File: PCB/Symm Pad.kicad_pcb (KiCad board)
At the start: 2 copper layers, 74 x 64.3 mm, 21 parts, among them J1 0.91"_OLED_Display, SW1 SW_Push, SW2 SW_Push, SW3 SW_Push, SW4 SW_Push, SW5 SW_Push, SW6 SW_Push, SW7 RotaryEncoder_Switch, U1 XIAO-RP2040-DIP

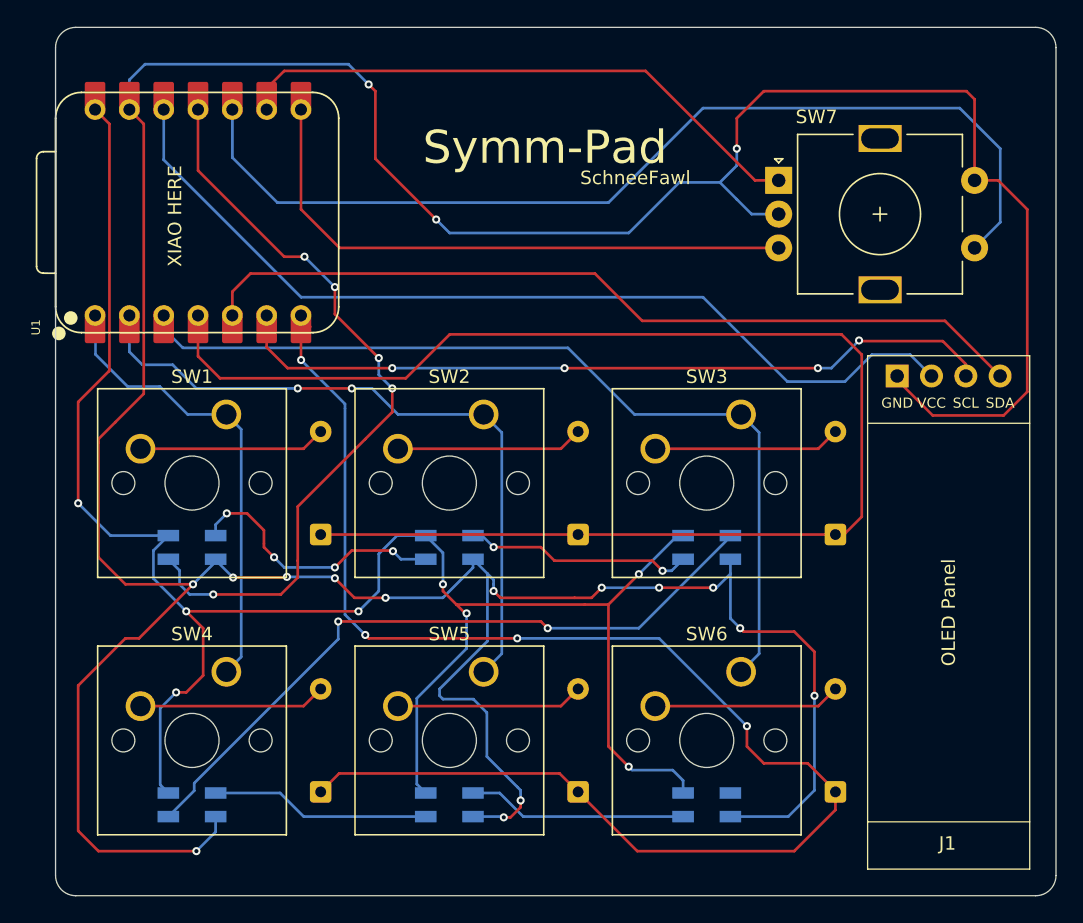
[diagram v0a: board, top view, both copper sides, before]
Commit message: Cleaned up tracks and vias
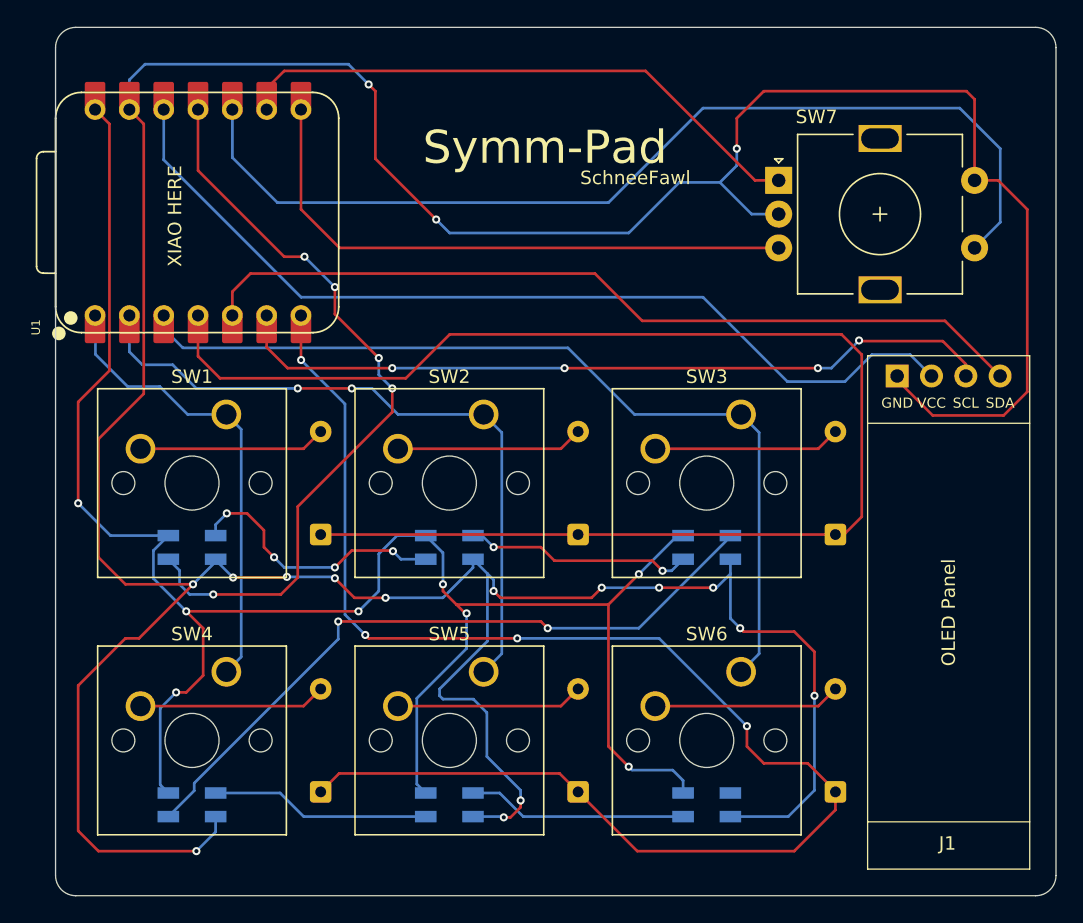
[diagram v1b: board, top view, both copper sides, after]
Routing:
- net Row 1: track 110.5 -> 109.8 mm
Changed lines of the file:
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@@
 	)
 	(segment
-		(start 78.75 55)
+		(start 78.5 55)
 		(end 81.5 55)
 		(width 0.2)
@@
 	)
 	(segment
-		(start 78.5 55)
-		(end 78.75 55)
-		(width 0.2)
-		(layer "F.Cu")
-		(net 1)
-	)
-	(segment
-		(start 72 54.5)
-		(end 72 54.75)
-		(width 0.2)
-		(layer "F.Cu")
-		(net 1)
-	)
-	(segment
 		(start 69.25 52.25)
 		(end 70.75 52.25)
@@
 	(segment
 		(start 72 53.5)
-		(end 72 54.5)
+		(end 72 54.75)
 		(width 0.2)
 		(layer "F.Cu")
@@
 	)
 	(segment
-		(start 59.75 46.75)
-		(end 59.75 47)
-		(width 0.2)
-		(layer "F.Cu")
-		(net 2)
-	)
-	(segment
 		(start 90.25 74.75)
 		(end 89.75 74.75)
@@
 	)
 	(segment
-		(start 61 45.5)
-		(end 59.75 46.75)
-		(width 0.2)
-		(layer "F.Cu")
-		(net 2)
-	)
-	(segment
 		(start 62.04 22.36)
 		(end 63.103 23.423)
@@
 	)
 	(segment
-		(start 63.103 43.397)
-		(end 61 45.5)
+		(start 59.75 46.75)
+		(end 63.103 43.397)
 		(width 0.2)
 		(layer "F.Cu")
@@
 	)
 	(segment
-		(start 95 58.5)
+		(start 89.5 58.5)
 		(end 96.25 58.5)
 		(width 0.2)
@@
 	)
 	(segment
-		(start 59.75 47)
+		(start 59.75 46.75)
 		(end 59.75 55.5)
 		(width 0.2)
@@
 	)
 	(segment
-		(start 89.5 58.5)
-		(end 95 58.5)
-		(width 0.2)
-		(layer "F.Cu")
-		(net 2)
-	)
-	(segment
 		(start 62.75 61.5)
 		(end 61.75 61.5)
@@
 	)
 	(segment
-		(start 90.75 72.5)
+		(start 88.5 70.25)
 		(end 91 72.75)
 		(width 0.2)
@@
 	)
 	(segment
-		(start 107 29)
+		(start 105.75 27.75)
 		(end 108.1 30.1)
 		(width 0.2)
@@
 	)
 	(segment
-		(start 88.5 70.25)
-		(end 90.75 72.5)
-		(width 0.2)
-		(layer "B.Cu")
-		(net 2)
-	)
-	(segment
 		(start 85.25 66)
 		(end 87.5 66)
@@
 	(segment
 		(start 89 57.16875)
-		(end 89 57.5)
-		(width 0.2)
-		(layer "B.Cu")
-		(net 2)
-	)
-	(segment
-		(start 107 29)
-		(end 105.75 27.75)
+		(end 89 58)
 		(width 0.2)
 		(layer "B.Cu")
@@
 	)
 	(segment
-		(start 89 57.5)
-		(end 89 58)
-		(width 0.2)
-		(layer "B.Cu")
-		(net 2)
-	)
-	(segment
 		(start 85 65.75)
 		(end 85.25 66)
@@
 	)
 	(segment
-		(start 86.25 59)
-		(end 95.75 59)
-		(width 0.2)
-		(layer "F.Cu")
-		(net 3)
-	)
-	(segment
-		(start 67.5 61)
+		(start 67.5 60.75)
 		(end 67.5 64.25)
 		(width 0.2)
@@
 	)
 	(segment
-		(start 95.75 59)
+		(start 86.25 59)
 		(end 97.5 59)
 		(width 0.2)
@@
 	)
 	(segment
-		(start 60.563 41.687)
-		(end 60.5 41.75)
+		(start 58.25 44)
+		(end 60.563 41.687)
 		(width 0.2)
 		(layer "F.Cu")
@@
 	)
 	(segment
-		(start 67.5 60.75)
-		(end 67.5 61)
-		(width 0.2)
-		(layer "F.Cu")
-		(net 3)
-	)
-	(segment
 		(start 85.25 58)
 		(end 86.25 59)
@@
 		(net 3)
 	)
-	(segment
-		(start 60.5 41.75)
-		(end 58.25 44)
-		(width 0.2)
-		(layer "F.Cu")
-		(net 3)
-	)
 	(via
 		(at 79 59.5)
@@
 	)
 	(segment
-		(start 74.5 55.75)
+		(start 74.5 51.75)
 		(end 74.5 57)
 		(width 0.2)
@@
 	)
 	(segment
-		(start 81.5 44.75)
-		(end 79.5 46.75)
-		(width 0.2)
-		(layer "F.Cu")
-		(net 4)
-	)
-	(segment
 		(start 67.12 22.36)
 		(end 67.12 26.87)
@@
 	)
 	(segment
-		(start 79.5 46.75)
-		(end 74.5 51.75)
+		(start 74.5 51.75)
+		(end 81.5 44.75)
 		(width 0.2)
 		(layer "F.Cu")
@@
 	)
 	(segment
-		(start 74.5 51.75)
-		(end 74.5 55.75)
-		(width 0.2)
-		(layer "F.Cu")
-		(net 4)
-	)
-	(segment
 		(start 81.5 43)
 		(end 81.5 44.75)
@@
 	)
 	(segment
-		(start 75.435 38.435)
-		(end 74.74 38.435)
-		(width 0.2)
-		(layer "F.Cu")
-		(net 25)
-	)
-	(segment
 		(start 74.75 40.9)
 		(end 74.74 40.89)
@@
 	(segment
 		(start 78 59.75)
-		(end 78 44.5)
+		(end 78 44.15)
 		(width 0.2)
 		(layer "B.Cu")
@@
 		(width 0.2)
 		(layer "B.Cu")
-		(net 25)
-	)
-	(segment
-		(start 78 44.5)
-		(end 78 44.15)
-		(width 0.2)
-		(layer "B.Cu")

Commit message: Correct footprint of neopixels
Earlier the SK6812 MINI footprint was being used which wasn't correct. Now changed to SK6812 MINI-E footprints.
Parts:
- removed D1, D2, D3, D4, D5, D6: SK6812MINI, LED_SMD:LED_SK6812MINI_PLCC4_3.5x3.5mm_P1.75mm
- added D13: SK6812MINI-E, kicad-keyboard-parts:MX_SK6812MINI-E, F.Cu at (66.7, 50.0)
- added D14: SK6812MINI-E, kicad-keyboard-parts:MX_SK6812MINI-E, F.Cu at (85.7, 50.0)
- added D15: SK6812MINI-E, kicad-keyboard-parts:MX_SK6812MINI-E, F.Cu at (104.8, 50.0)
- added D16: SK6812MINI-E, kicad-keyboard-parts:MX_SK6812MINI-E, F.Cu at (66.7, 69.1)
- added D17: SK6812MINI-E, kicad-keyboard-parts:MX_SK6812MINI-E, F.Cu at (85.7, 69.1)
- added D18: SK6812MINI-E, kicad-keyboard-parts:MX_SK6812MINI-E, F.Cu at (104.8, 69.1)
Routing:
- net Net-(D3-DOUT): track 51.8 -> 0.00 mm, vias 2 -> 0
- net Net-(D15-DOUT): track 0.00 -> 45.6 mm, vias 0 -> 2
- net Net-(D16-DOUT): track 0.00 -> 36.7 mm, vias 0 -> 2
- net Net-(D17-DOUT): track 0.00 -> 33.9 mm, vias 0 -> 2
- net Net-(D13-DOUT): track 0.00 -> 30.3 mm, vias 0 -> 2
- net Net-(D14-DOUT): track 0.00 -> 30.0 mm, vias 0 -> 2
- net Row 0: track 106.6 -> 128.6 mm, vias 0 -> 4
- net +5V: track 141.9 -> 162.3 mm, vias 8 -> 12
- net Net-(D1-DOUT): track 19.9 -> 0.00 mm, vias 4 -> 0
- net Net-(D2-DOUT): track 17.0 -> 0.00 mm, vias 2 -> 0
- net Net-(D5-DOUT): track 16.3 -> 0.00 mm
- net Net-(D4-DOUT): track 16.3 -> 0.00 mm
- net Net-(D13-DIN): track 56.2 -> 46.5 mm
- net GND: track 300.2 -> 295.3 mm, vias 17 -> 13
- net Col 0: track 33.9 -> 34.8 mm
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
